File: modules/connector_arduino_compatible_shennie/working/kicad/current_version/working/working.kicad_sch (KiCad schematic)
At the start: 1 part, among them U1 bbat328

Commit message: gitignore update mainly and update
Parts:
- added 111, 1111: nt2, nt2_electronic_nettie_2_nets_smd, symbol oomlout_oomp_part_symbols:nt2_electronic_nettie_2_nets_smd
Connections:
- net pd0: now also 1111.1
- net pd1: now also 111.1
- new net rx_xxxx: 1111.2
- new net tx_xxxx: 111.2
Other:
- note added: "do not change this side tx to tx because it's a connector"
- note added: "i2c"
- note added: "name"
- note added: "oomp connector arduino_compatible shennie"
- note added: "patched elsewhere block name"
- note added: "shennie_con"
- note added: "shennie_con_tx_rx_patch_block"
- note removed: "module connector arduino_compatible shennie"
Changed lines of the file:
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@@
   (junction (at 147.32 87.63) (diameter 0) (color 0 0 0 0)
   )
-  (junction (at 115.57 81.28) (diameter 0) (color 0 0 0 0)
-  )
-  (junction (at 114.3 87.63) (diameter 0) (color 0 0 0 0)
-  )
   (junction (at 133.35 128.27) (diameter 0) (color 0 0 0 0)
   )
+  (wire (pts (xy 132.08 148.59) (xy 135.89 148.59))
+    (stroke (width 0) (type default))
+  )
   (wire (pts (xy 135.89 128.27) (xy 135.89 125.73))
     (stroke (width 0) (type default))
@@
     (stroke (width 0) (type default))
   )
+  (wire (pts (xy 113.03 85.09) (xy 120.65 85.09))
+    (stroke (width 0) (type default))
+  )
   (wire (pts (xy 146.05 102.87) (xy 148.59 102.87))
     (stroke (width 0) (type default))
   )
-  (wire (pts (xy 115.57 85.09) (xy 120.65 85.09))
-    (stroke (width 0) (type default))
-  )
-  (wire (pts (xy 114.3 85.09) (xy 114.3 87.63))
-    (stroke (width 0) (type default))
-  )
   (wire (pts (xy 118.11 92.71) (xy 120.65 92.71))
     (stroke (width 0) (type default))
   )
+  (wire (pts (xy 132.08 154.94) (xy 135.89 154.94))
+    (stroke (width 0) (type default))
+  )
   (wire (pts (xy 146.05 107.95) (xy 148.59 107.95))
     (stroke (width 0) (type default))
@@
     (stroke (width 0) (type default))
   )
+  (wire (pts (xy 123.19 148.59) (xy 127 148.59))
+    (stroke (width 0) (type default))
+  )
   (wire (pts (xy 118.11 110.49) (xy 120.65 110.49))
     (stroke (width 0) (type default))
@@
     (stroke (width 0) (type default))
   )
-  (wire (pts (xy 115.57 81.28) (xy 115.57 85.09))
+  (wire (pts (xy 113.03 87.63) (xy 120.65 87.63))
     (stroke (width 0) (type default))
   )
@@
     (stroke (width 0) (type default))
   )
-  (wire (pts (xy 113.03 81.28) (xy 115.57 81.28))
-    (stroke (width 0) (type default))
-  )
   (wire (pts (xy 118.11 97.79) (xy 120.65 97.79))
     (stroke (width 0) (type default))
   )
-  (wire (pts (xy 113.03 85.09) (xy 114.3 85.09))
-    (stroke (width 0) (type default))
-  )
   (wire (pts (xy 146.05 100.33) (xy 148.59 100.33))
     (stroke (width 0) (type default))
   )
-  (wire (pts (xy 115.57 78.74) (xy 113.03 78.74))
+  (wire (pts (xy 123.19 154.94) (xy 127 154.94))
     (stroke (width 0) (type default))
   )
@@
     (stroke (width 0) (type default))
   )
-  (wire (pts (xy 113.03 87.63) (xy 114.3 87.63))
-    (stroke (width 0) (type default))
-  )
   (wire (pts (xy 118.11 105.41) (xy 120.65 105.41))
     (stroke (width 0) (type default))
@@
     (stroke (width 0) (type default))
   )
-  (wire (pts (xy 115.57 78.74) (xy 115.57 81.28))
-    (stroke (width 0) (type default))
-  )
-  (wire (pts (xy 114.3 87.63) (xy 120.65 87.63))
-    (stroke (width 0) (type default))
-  )
   (wire (pts (xy 147.32 85.09) (xy 147.32 87.63))
     (stroke (width 0) (type default))
@@
     (stroke (width 0) (type default))
   )
-  (rectangle (start 97.79 48.26) (end 161.29 137.16)
+  (rectangle (start 134.62 144.78) (end 160.02 157.48)
+    (stroke (width 0.5) (type default))
+    (fill (type none))
+  )
+  (rectangle (start 97.79 137.16) (end 161.29 162.56)
+    (stroke (width 0) (type default))
+    (fill (type none))
+  )
+  (rectangle (start 99.06 144.78) (end 124.46 157.48)
+    (stroke (width 0.5) (type default))
+    (fill (type none))
+  )
+  (rectangle (start 97.79 48.26) (end 161.29 162.56)
     (stroke (width 1) (type default))
     (fill (type none))
   )
-  (text "module\nconnector\narduino_compatible\nshennie\n" (at 99.06 64.77 0)
+  (rectangle (start 81.28 86.36) (end 81.28 86.36)
+    (stroke (width 0) (type default))
+    (fill (type none))
+  )
+  (rectangle (start 147.32 144.78) (end 160.02 157.48)
+    (stroke (width 0.5) (type default))
+    (fill (type none))
+  )
+  (rectangle (start 123.19 48.26) (end 161.29 54.61)
+    (stroke (width 1) (type default))
+    (fill (type color) (color 0 0 0 0))
+  )
+  (text "do not change\nthis side\n\ntx to tx\nbecause it's a\nconnector\n"
+    (at 101.6 154.94 0)
+    (effects (font (size 0.75 0.75)) (justify left bottom))
+  )
+  (text "shennie_con_tx_rx_patch_block" (at 99.06 140.97 0)
+    (effects (font (size 1.5 1.5)) (justify left bottom))
+  )
+  (text "oomp\nconnector\narduino_compatible\nshennie" (at 99.06 64.77 0)
     (effects (font (size 2.5 2.5)) (justify left bottom))
   )
+  (text "patched \nelsewhere\nblock \nname\n" (at 149.86 151.13 0)
+    (effects (font (size 0.75 0.75)) (justify left bottom))
+  )
+  (text "i2c\n" (at 77.47 100.33 90)
+    (effects (font (size 1.27 1.27)) (justify left bottom))
+  )
+  (text "shennie_con" (at 160.02 54.61 0)
+    (effects (font (size 3.5 3.5) (thickness 0.8) bold (color 255 255 255 1)) (justify right bottom))
+  )
+  (text "name" (at 125.73 54.61 90)
+    (effects (font (size 1.27 1.27) (thickness 0.254) bold (color 255 255 255 1)) (justify left bottom))
+  )
   (label "reset" (at 148.59 87.63 0) (fields_autoplaced)
     (effects (font (size 1.27 1.27)) (justify left bottom))
@@
     (effects (font (size 1.27 1.27)) (justify right bottom))
   )
+  (label "rx_shennie" (at 123.19 154.94 180) (fields_autoplaced)
+    (effects (font (size 1.27 1.27)) (justify right bottom))
+  )
   (label "pd2" (at 118.11 90.17 180) (fields_autoplaced)
     (effects (font (size 1.27 1.27)) (justify right bottom))
@@
     (effects (font (size 1.27 1.27)) (justify right bottom))
   )
-  (label "tx_secondary" (at 113.03 87.63 180) (fields_autoplaced)
+  (label "tx_shennie" (at 113.03 87.63 180) (fields_autoplaced)
     (effects (font (size 1.27 1.27)) (justify right bottom))
   )
@@
     (effects (font (size 1.27 1.27)) (justify right bottom))
   )
-  (label "rx_secondary" (at 113.03 81.28 180) (fields_autoplaced)
+  (label "rx_shennie" (at 113.03 85.09 180) (fields_autoplaced)
     (effects (font (size 1.27 1.27)) (justify right bottom))
   )
@@
     (effects (font (size 1.27 1.27)) (justify left bottom))
   )
-  (label "pd1" (at 113.03 85.09 180) (fields_autoplaced)
+  (label "pd1" (at 118.11 87.63 180) (fields_autoplaced)
     (effects (font (size 1.27 1.27)) (justify right bottom))
   )
@@
     (effects (font (size 1.27 1.27)) (justify left bottom))
   )
+  (label "tx_shennie" (at 123.19 148.59 180) (fields_autoplaced)
+    (effects (font (size 1.27 1.27)) (justify right bottom))
+  )
   (label "pc5" (at 148.59 113.03 0) (fields_autoplaced)
     (effects (font (size 1.27 1.27)) (justify left bottom))
@@
     (effects (font (size 1.27 1.27)) (justify right bottom))
   )
+  (label "tx_xxxx" (at 135.89 148.59 0) (fields_autoplaced)
+    (effects (font (size 1.27 1.27)) (justify left bottom))
+  )
   (label "pd7" (at 118.11 102.87 180) (fields_autoplaced)
     (effects (font (size 1.27 1.27)) (justify right bottom))
@@
     (effects (font (size 1.27 1.27)) (justify right bottom))
   )
+  (label "rx_xxxx" (at 135.89 154.94 0) (fields_autoplaced)
+    (effects (font (size 1.27 1.27)) (justify left bottom))
+  )
   (label "pb3" (at 118.11 113.03 180) (fields_autoplaced)
     (effects (font (size 1.27 1.27)) (justify right bottom))
   )
-  (label "pd0" (at 113.03 78.74 180) (fields_autoplaced)
+  (label "pd0" (at 118.11 85.09 180) (fields_autoplaced)
     (effects (font (size 1.27 1.27)) (justify right bottom))
   )
@@
     )
   )
+  (symbol (lib_id "oomlout_oomp_part_symbols:nt2_electronic_nettie_2_nets_smd") (at 129.54 154.94 0) (unit 1)
+    (in_bom no) (on_board yes) (dnp no) (fields_autoplaced)
+    (property "Reference" "1111" (at 129.54 149.86 0)
+      (effects (font (size 1.27 1.27)))
+    )
+    (property "Value" "nt2" (at 129.54 152.4 0)
+      (effects (font (size 1.27 1.27)))
+    )
+    (property "Footprint" "nt2_electronic_nettie_2_nets_smd" (at 129.54 154.94 0)
+      (effects (font (size 1.27 1.27)) hide)
+    )
+    (property "Datasheet" "https://github.com/oomlout/oomlout_oomp_v3/parts/electronic_nettie_2_nets_smd/datasheet.pdf" (at 129.54 154.94 0)
+      (effects (font (size 1.27 1.27)) hide)
+    )
+    (pin "1")
+    (pin "2")
+    (instances
+      (project "working"
+        (path "/202b97fb-0be0-4d23-9dac-1f48691efef5"
+          (reference "1111") (unit 1)
+        )
+      )
+      (project "working"
+        (path "/c9993764-076f-44f6-bf4c-6b69ce17c9e4"
+          (reference "11") (unit 1)
+        )
+      )
+    )
+  )
   (symbol (lib_id "power:+5V") (at 140.97 72.39 0) (unit 1)
     (in_bom yes) (on_board yes) (dnp no)
@@
         )
       )
+    )
+  )
+  (symbol (lib_id "oomlout_oomp_part_symbols:nt2_electronic_nettie_2_nets_smd") (at 129.54 148.59 0) (unit 1)
+    (in_bom no) (on_board yes) (dnp no) (fields_autoplaced)
+    (property "Reference" "111" (at 129.54 143.51 0)
+      (effects (font (size 1.27 1.27)))
+    )
+    (property "Value" "nt2" (at 129.54 146.05 0)
+      (effects (font (size 1.27 1.27)))
+    )
+    (property "Footprint" "nt2_electronic_nettie_2_nets_smd" (at 129.54 148.59 0)
+      (effects (font (size 1.27 1.27)) hide)
+    )
+    (property "Datasheet" "https://github.com/oomlout/oomlout_oomp_v3/parts/electronic_nettie_2_nets_smd/datasheet.pdf" (at 129.54 148.59 0)
+      (effects (font (size 1.27 1.27)) hide)
+    )
+    (pin "1")
+    (pin "2")
+    (instances
+      (project "working"
+        (path "/202b97fb-0be0-4d23-9dac-1f48691efef5"
+          (reference "111") (unit 1)
+        )
+      )
+      (project "working"
+        (path "/c9993764-076f-44f6-bf4c-6b69ce17c9e4"
+          (reference "1") (unit 1)
+        )
+      )

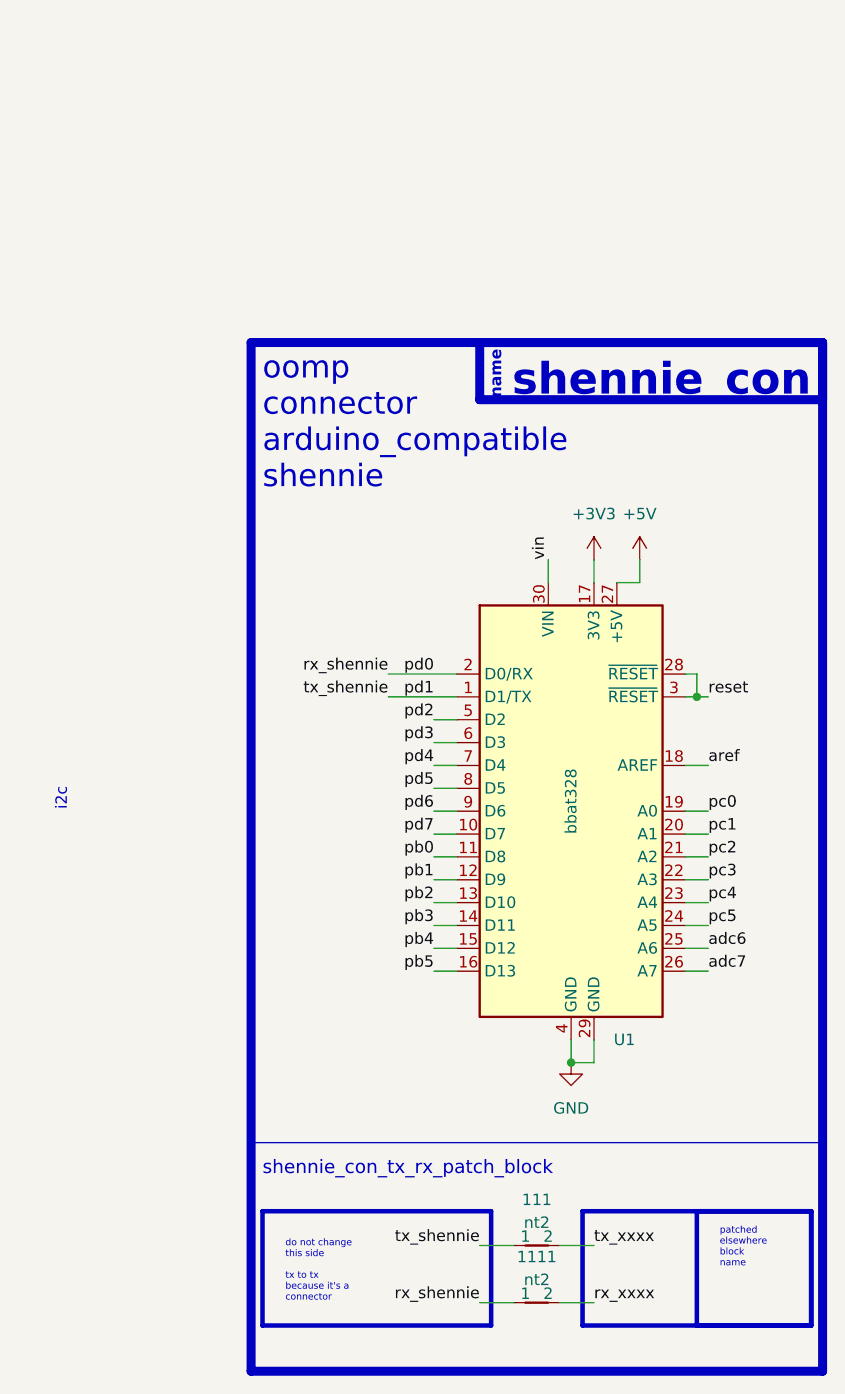
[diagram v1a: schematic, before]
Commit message: fixed formatting to be more consistent
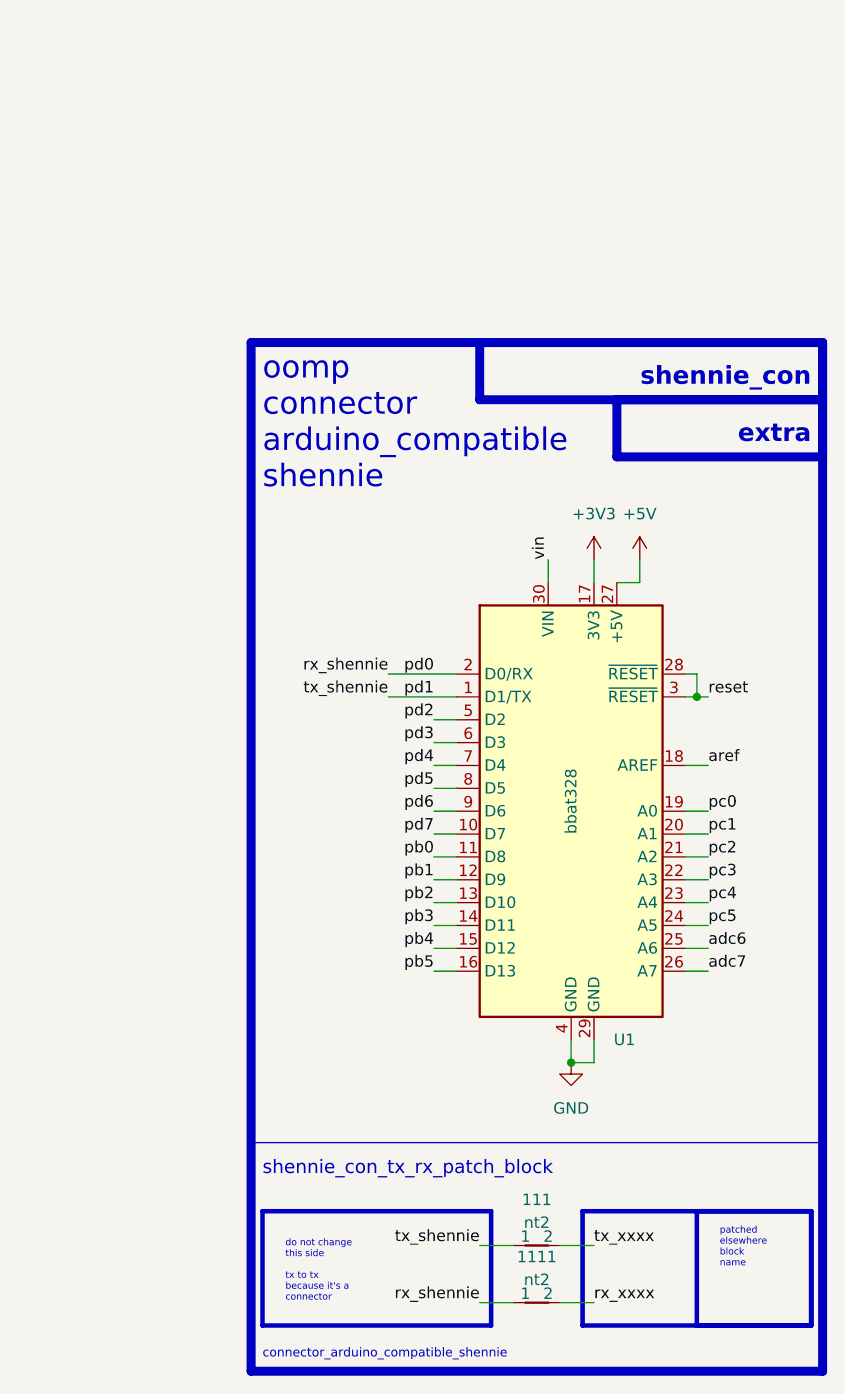
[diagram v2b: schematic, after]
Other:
- note added: "connector_arduino_compatible_shennie"
- note added: "extra"
- note removed: "i2c"
- note removed: "name"
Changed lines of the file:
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@@
     (stroke (width 0) (type default))
+  )
+  (rectangle (start 138.43 54.61) (end 161.29 60.96)
+    (stroke (width 1) (type default))
+    (fill (type none))
   )
   (rectangle (start 134.62 144.78) (end 160.02 157.48)
@@
   (rectangle (start 123.19 48.26) (end 161.29 54.61)
     (stroke (width 1) (type default))
-    (fill (type color) (color 0 0 0 0))
+    (fill (type none))
   )
   (text "do not change\nthis side\n\ntx to tx\nbecause it's a\nconnector\n"
@@
     (effects (font (size 1.5 1.5)) (justify left bottom))
   )
+  (text "extra" (at 160.02 59.69 0)
+    (effects (font (size 2 2) (thickness 0.8) bold) (justify right bottom))
+  )
   (text "oomp\nconnector\narduino_compatible\nshennie" (at 99.06 64.77 0)
     (effects (font (size 2.5 2.5)) (justify left bottom))
@@
     (effects (font (size 0.75 0.75)) (justify left bottom))
   )
-  (text "i2c\n" (at 77.47 100.33 90)
-    (effects (font (size 1.27 1.27)) (justify left bottom))
+  (text "shennie_con" (at 160.02 53.34 0)
+    (effects (font (size 2 2) (thickness 0.8) bold) (justify right bottom))
   )
-  (text "shennie_con" (at 160.02 54.61 0)
-    (effects (font (size 3.5 3.5) (thickness 0.8) bold (color 255 255 255 1)) (justify right bottom))
-  )
-  (text "name" (at 125.73 54.61 90)
-    (effects (font (size 1.27 1.27) (thickness 0.254) bold (color 255 255 255 1)) (justify left bottom))
+  (text "connector_arduino_compatible_shennie" (at 99.06 161.29 0)
+    (effects (font (size 1 1)) (justify left bottom))
   )
   (label "reset" (at 148.59 87.63 0) (fields_autoplaced)

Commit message: schematic formatting
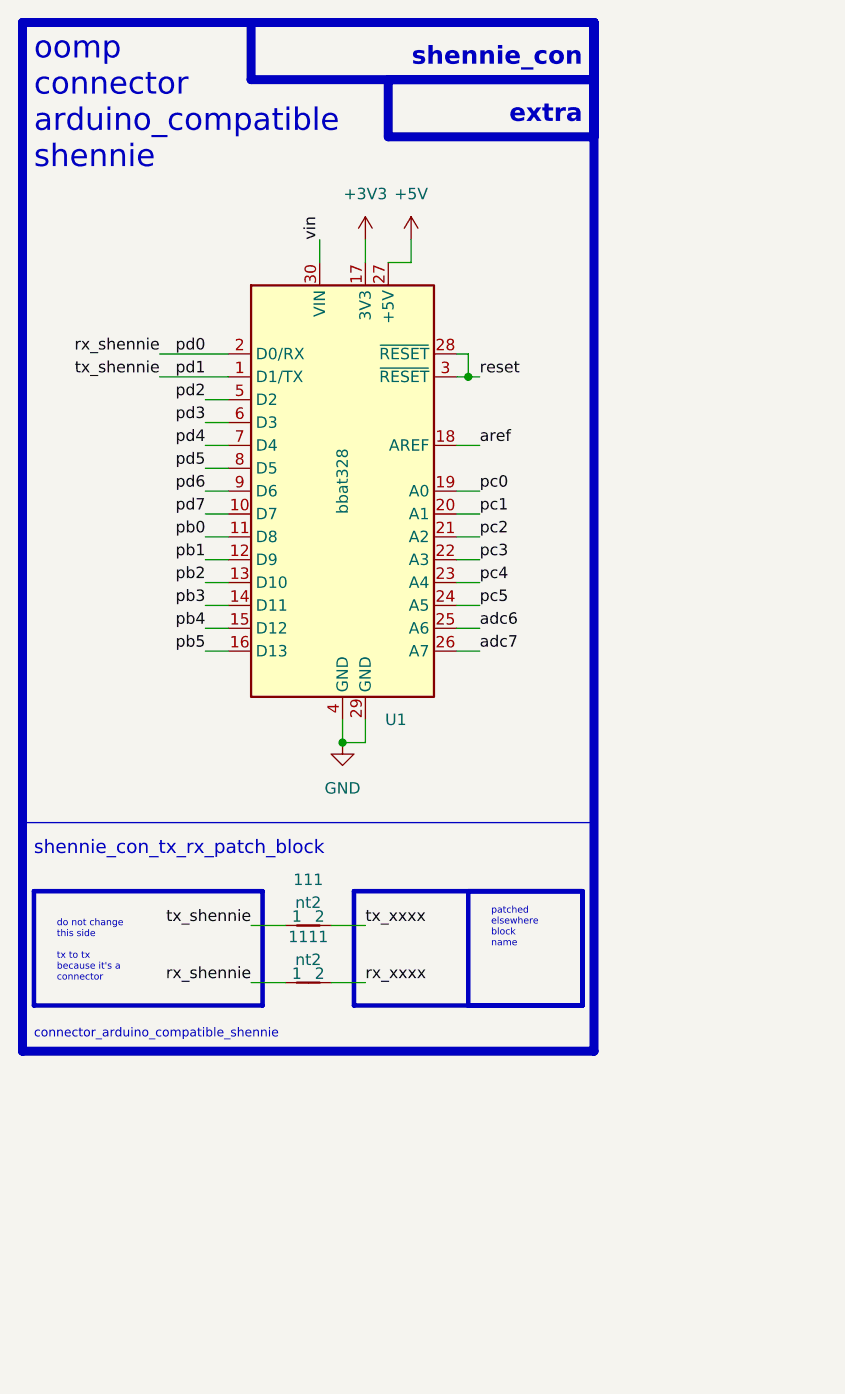
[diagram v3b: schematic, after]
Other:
- moved on the sheet: 111, 1111, U1
